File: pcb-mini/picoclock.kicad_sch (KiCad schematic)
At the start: 85 parts, among them J1 UART, J10 USB, J12 LED_5V, J14 SJ2-35863B1-SMT-TR, J2 USB_A, J3 UART, J4 xx, J5 Micro_SD_Card_Det1, J6 USB_C_Receptacle, J7 DBG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

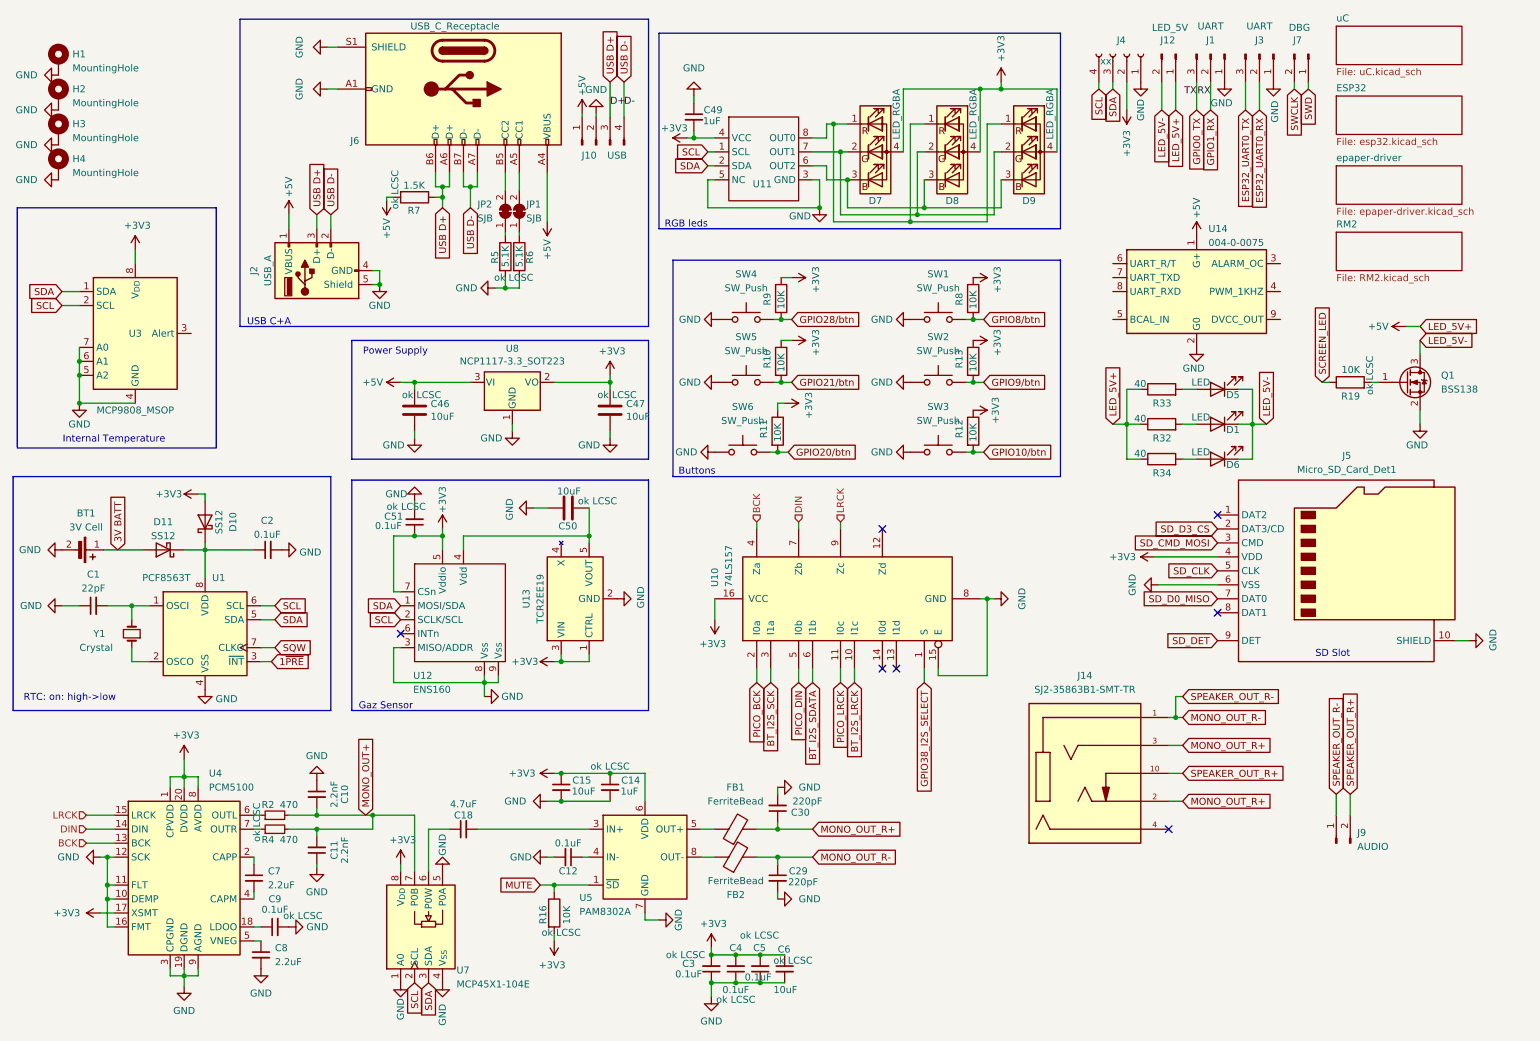
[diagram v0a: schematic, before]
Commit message: [pcb] mini: add SHT40 + senseair S88 connectors
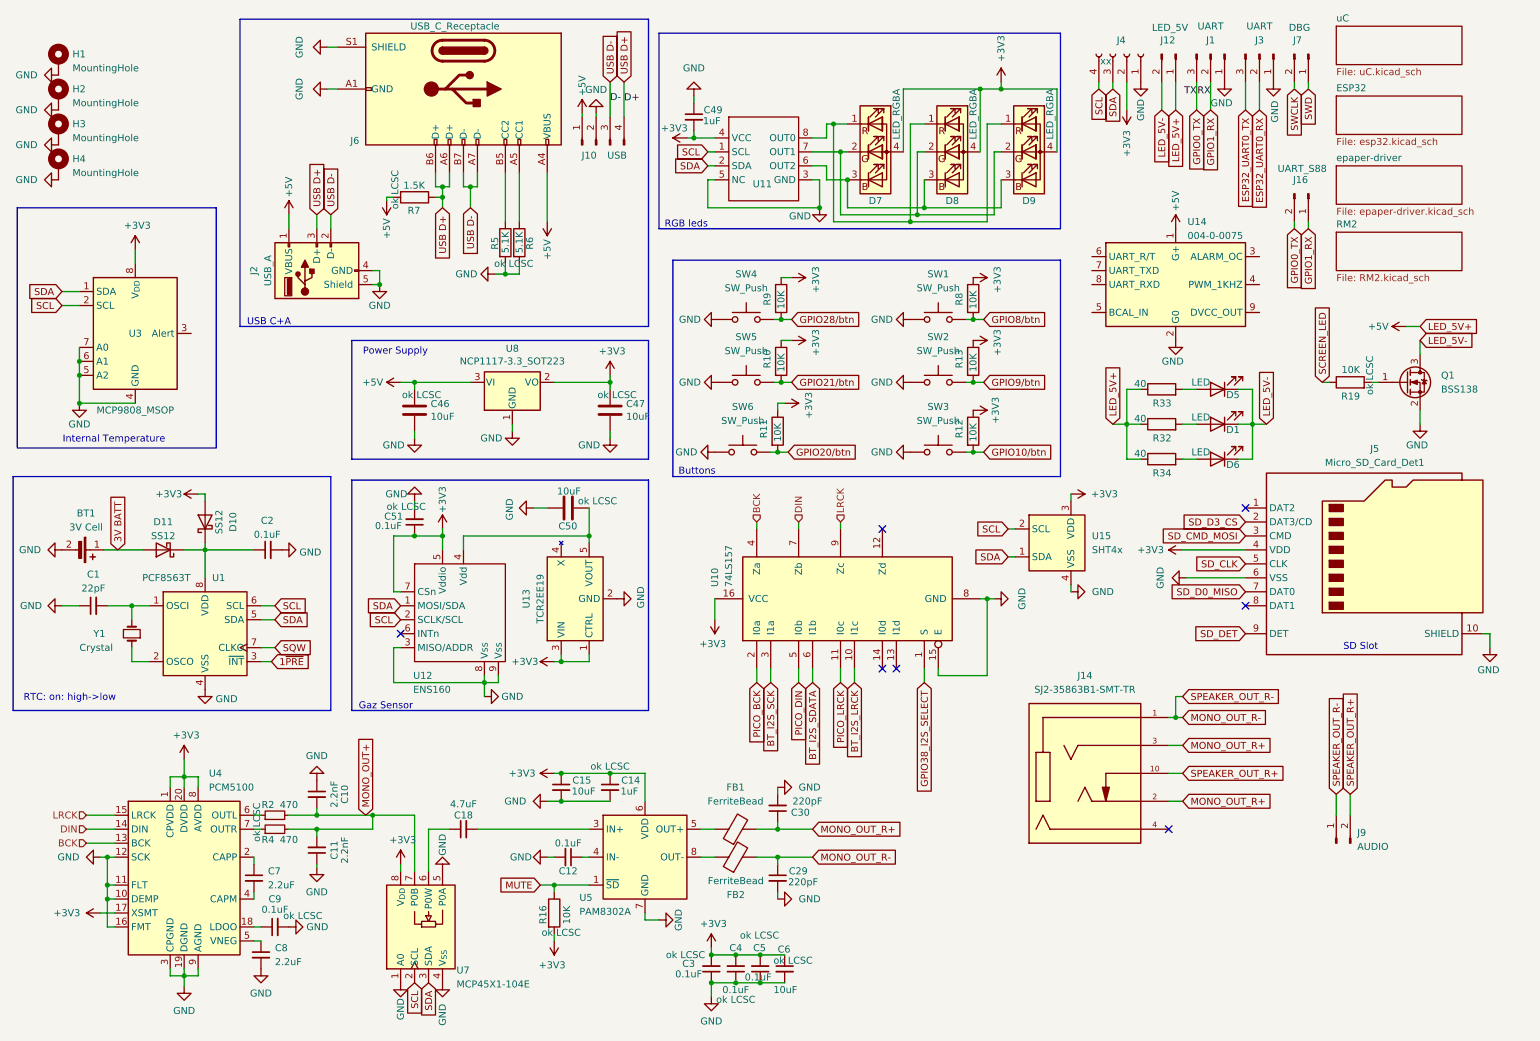
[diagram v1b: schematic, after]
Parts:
- removed JP1, JP2: SJB, Jumper:SolderJumper-2_P1.3mm_Bridged_RoundedPad1.0x1.5mm, symbol Jumper:SolderJumper_2_Bridged
- added J16: UART_S88, Connector_PinHeader_2.54mm:PinHeader_1x02_P2.54mm_Vertical, symbol Connector:Conn_01x02_Pin
- added U15: SHT4x, Sensor_Humidity:Sensirion_DFN-4_1.5x1.5mm_P0.8mm_SHT4x_NoCentralPad, symbol Sensor_Humidity:SHT4x
- U14: footprint senseair:Senseair_S8_Down -> (none); Footprint_disabled (none) -> senseair:Senseair_S8_Up
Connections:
- net +3V3: now also U15.3 (VDD)
- net GND: now also U15.4 (VSS)
- net GPIO0_TX: now also J16.2 (Pin_2)
- net GPIO1_RX: now also J16.1 (Pin_1)
- net SCL: now also U15.2 (SCL)
- net SDA: now also U15.1 (SDA)
- net USB D+: now also J10.4 (Pin_4); no longer J10.3 (Pin_3)
- net USB D-: now also J10.3 (Pin_3); no longer J10.4 (Pin_4)
- net at R6.1: now also J6.A5 (CC1)
- net at R5.1: now also J6.B5 (CC2)
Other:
- moved on the sheet: J5, R5, R6, U14

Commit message: [pcb] mini: move audio into dedicated sheet
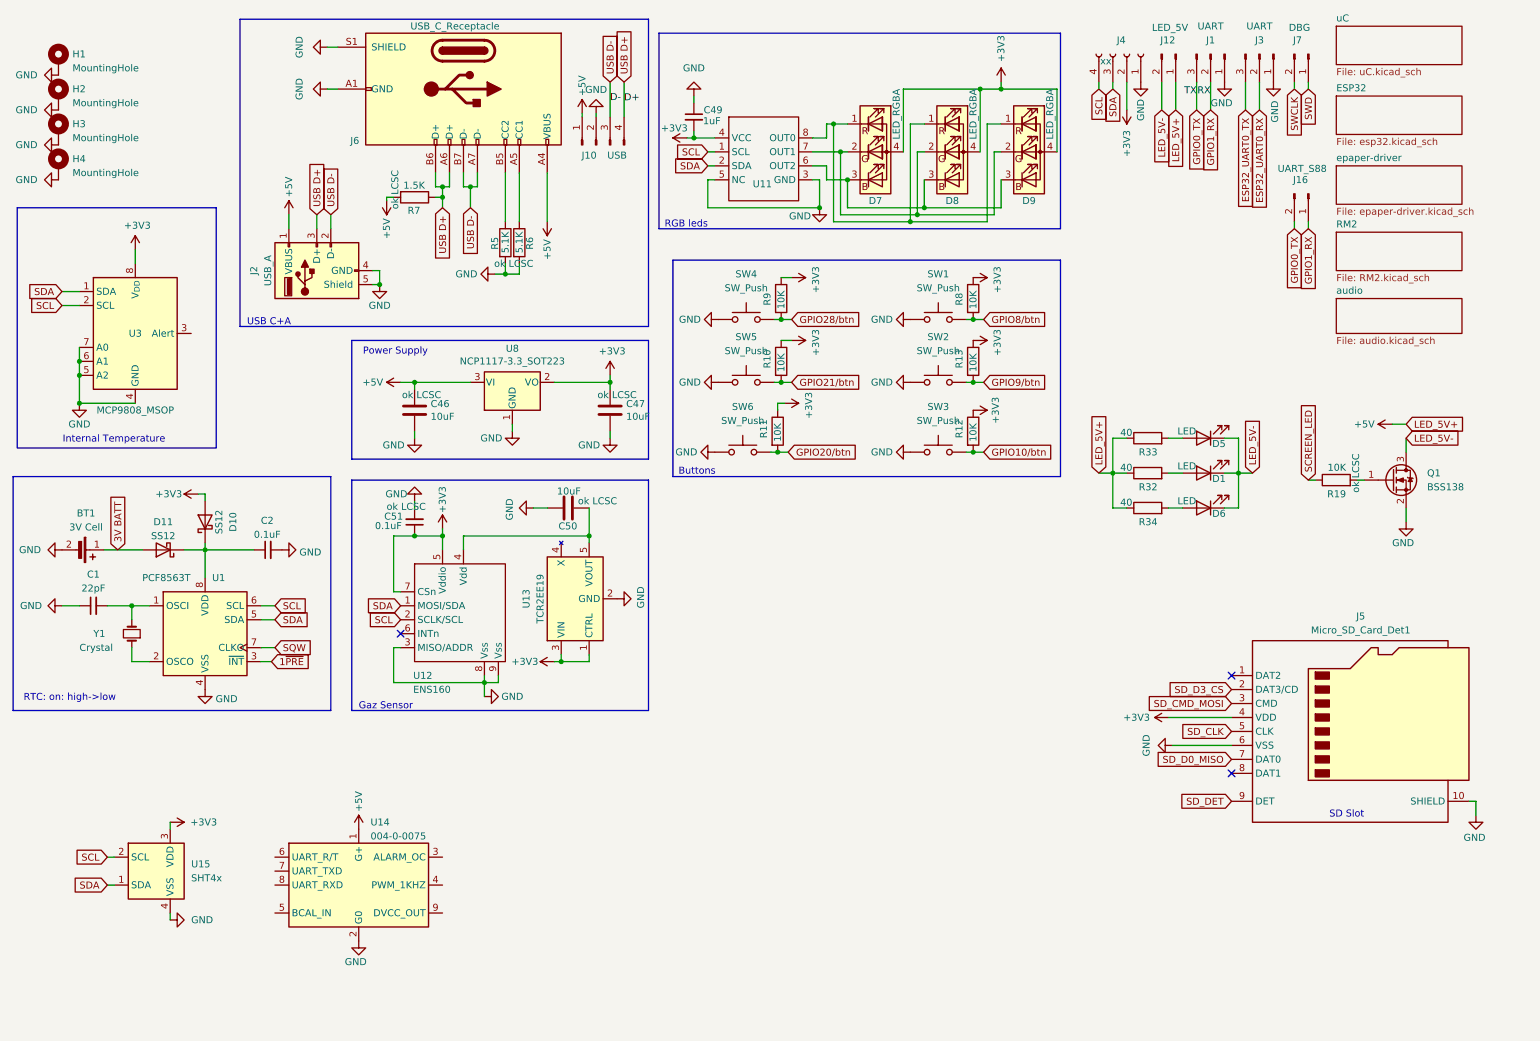
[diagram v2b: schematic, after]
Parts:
- removed C10, C11: 2.2nF, Capacitor_SMD:C_0603_1608Metric, symbol Device:C_Small
- removed C12, C3, C4, C5, C9: 0.1uF, Capacitor_SMD:C_0603_1608Metric, symbol Device:C_Small
- removed C14: 1uF, Capacitor_SMD:C_0603_1608Metric, symbol Device:C_Small
- removed C15: 10uF, Capacitor_SMD:C_0603_1608Metric, symbol Device:C_Small
- removed C18: 4.7uF, Capacitor_SMD:C_0603_1608Metric, symbol Device:C_Small
- removed C29, C30: 220pF, Capacitor_SMD:C_0603_1608Metric, symbol Device:C_Small
- removed C6: 10uF, Capacitor_SMD:C_0805_2012Metric, symbol Device:C_Small
- removed C7: 2.2uF, Capacitor_SMD:C_0603_1608Metric, symbol Device:C_Small
- removed C8: 2.2uF, Capacitor_SMD:C_0402_1005Metric, symbol Device:C_Small
- removed FB1, FB2: FerriteBead, Inductor_SMD:L_0603_1608Metric, symbol Device:FerriteBead
- removed J14: SJ2-35863B1-SMT-TR, SJ2-35863B1-SMT-TR:CUI_SJ2-35863B1-SMT-TR, symbol SOP65P780X200-20N:SJ2-35863B1-SMT-TR
- removed J9: AUDIO, Connector_PinHeader_2.54mm:PinHeader_1x02_P2.54mm_Vertical, symbol Connector:Conn_01x02_Pin
- removed R16: 10K, Resistor_SMD:R_0402_1005Metric, symbol Device:R
- removed R2, R4: 470, Resistor_SMD:R_0603_1608Metric, symbol Device:R_Small
- removed U10: 74LS157, Package_SO:SOP-16_4.55x10.3mm_P1.27mm, symbol 74xx:74LS157
- removed U4: PCM5100, Package_SO:TSSOP-20_4.4x6.5mm_P0.65mm, symbol Audio:PCM5100
- removed U5: PAM8302A, Package_SO:SOP-8_3.76x4.96mm_P1.27mm, symbol Amplifier_Audio:PAM8302AAD
- removed U7: MCP45X1-104E, Package_SO:MSOP-8_3x3mm_P0.65mm, symbol Lunasys_Library:MCP4551T
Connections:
- no-connect marks 7 -> 3
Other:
- added sheet audio (audio.kicad_sch)
- moved on the sheet: D1, D5, D6, J5, Q1, R19, R32, R33, R34, U14, U15

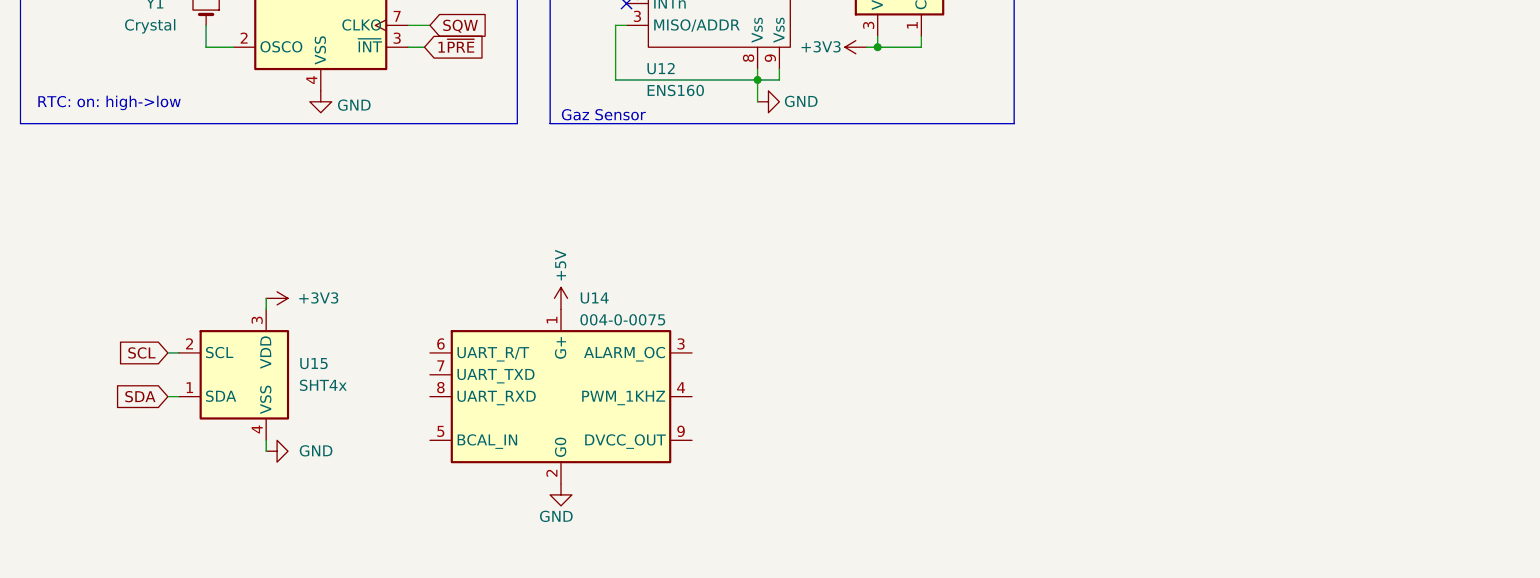
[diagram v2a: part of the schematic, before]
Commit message: [pcb] mini: add STCC4 and SCD41
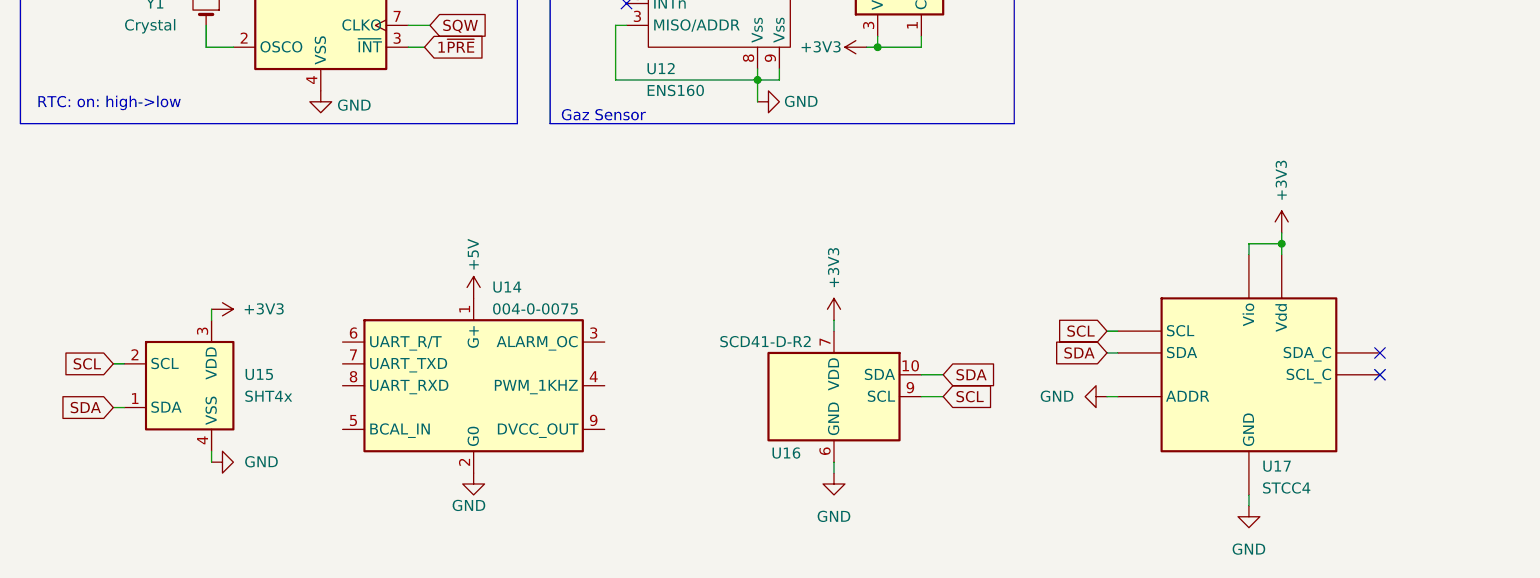
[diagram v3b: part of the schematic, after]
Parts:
- added U16: SCD41-D-R2, Sensor:Sensirion_SCD4x-1EP_10.1x10.1mm_P1.25mm_EP4.8x4.8mm, symbol Sensor_Gas:SCD41-D-R2
- added U17: STCC4, stcc4:STCC4, symbol Lunasys_Library:STCC4
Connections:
- net +3V3: now also U16.19 (VDD), U16.7 (VDD), U17.6 (Vio), U17.7 (Vdd)
- net GND: now also U16.20 (GND), U16.21 (GND), U16.6 (GND), U17.3 (ADDR), U17.4 (GND)
- net SCL: now also U16.9 (SCL), U17.1 (SCL)
- net SDA: now also U16.10 (SDA), U17.5 (SDA)
- no-connect marks 3 -> 5
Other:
- moved on the sheet: U14, U15

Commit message: [pcb] mini: add decoupling caps, improve power path of screen
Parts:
- added C52, C54, C55: 0.1uF, Capacitor_SMD:C_0603_1608Metric, symbol Device:C_Small
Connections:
- net +3V3: now also C52.1, C54.1, C55.1
- net GND: now also C52.2, C54.2, C55.2

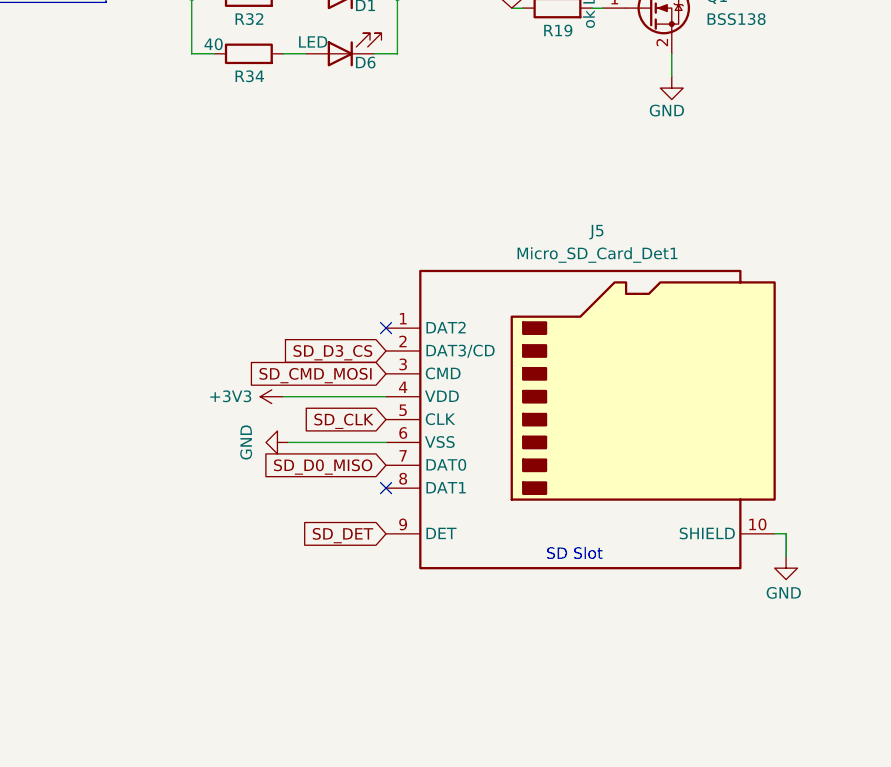
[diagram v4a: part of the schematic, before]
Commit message: [pcb] fix SD card detection (add pullup) + improve footprint
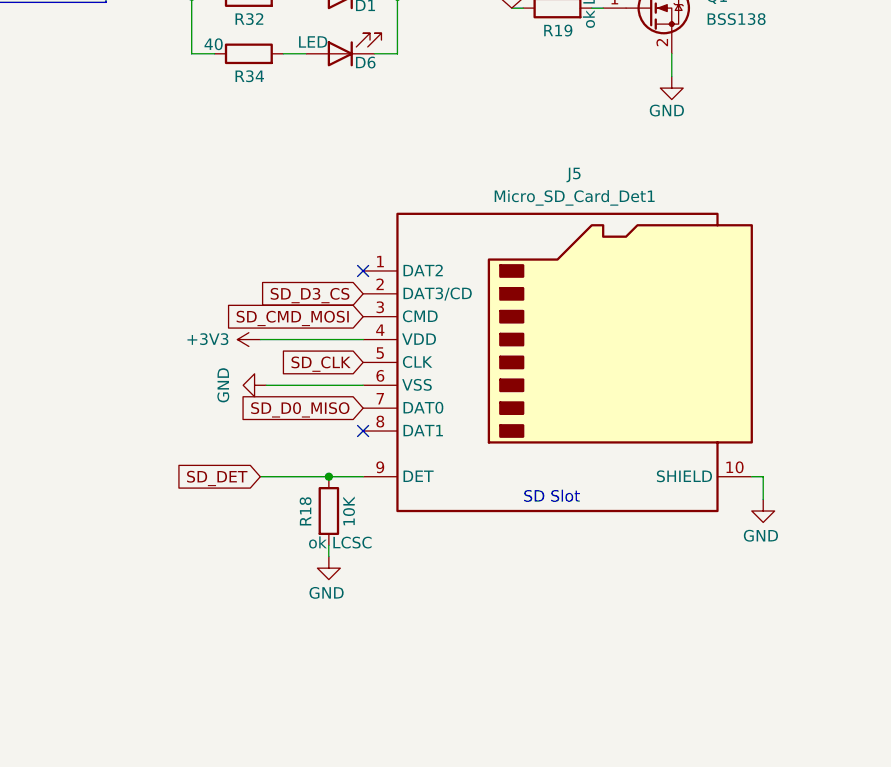
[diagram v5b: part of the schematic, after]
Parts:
- added R18: 10K, Resistor_SMD:R_0402_1005Metric, symbol Device:R
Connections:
- net GND: now also R18.2
- net SD_DET: now also R18.1
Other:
- moved on the sheet: J5
